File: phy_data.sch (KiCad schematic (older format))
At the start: 18 parts

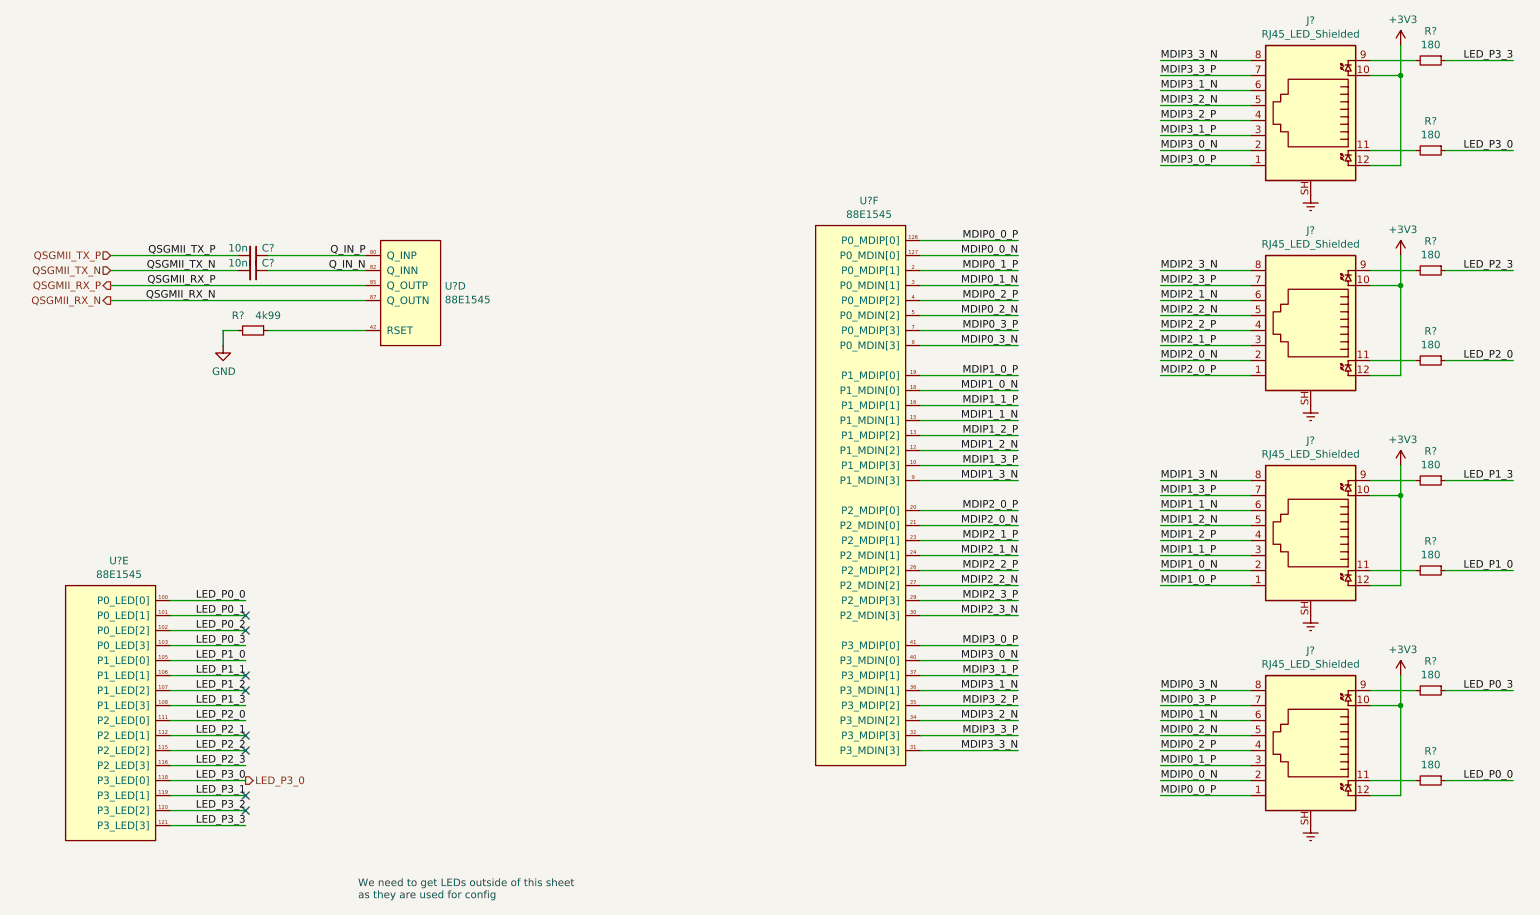
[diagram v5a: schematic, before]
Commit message: sch: Annotate & associate symbols with footprints
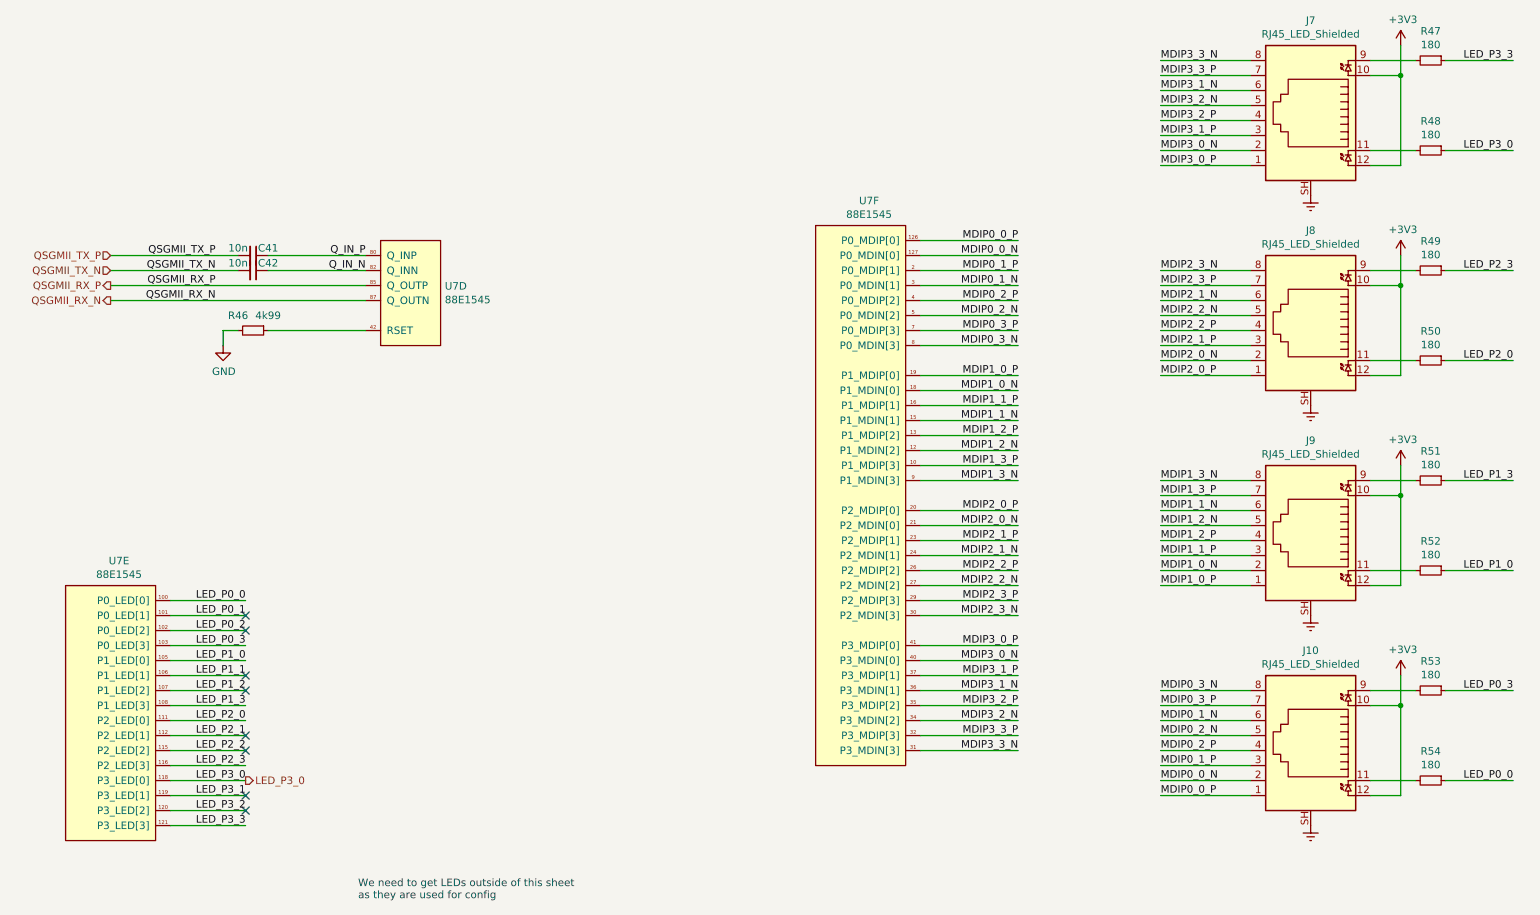
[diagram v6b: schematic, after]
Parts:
- C41, C42: renamed from C?; footprint (none) -> Capacitor_SMD:C_0402_1005Metric
- R46, R47, R48, R49, R50, R51, R52, R53, R54: renamed from R?; footprint (none) -> Resistor_SMD:R_0603_1608Metric
- gave numbers to parts that had none: 5
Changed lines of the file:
@@
 $EndDescr
 $Comp
-L pimouss-motherboard:88E1545 U?
+L pimouss-motherboard:88E1545 U7
 U 4 1 5C7D3D27
 P 3400 2100
-F 0 "U?" H 3828 1796 50  0000 L CNN
+F 0 "U7" H 3828 1796 50  0000 L CNN
 F 1 "88E1545" H 3828 1705 50  0000 L CNN
 F 2 "pimouss-motherboard:LQFP-128-1EP_14x20mm_P0.5mm_EP3.93x6.42mm" H 4850 -300 50  0001 C CNN
@@
 $EndComp
 $Comp
-L pimouss-motherboard:88E1545 U?
+L pimouss-motherboard:88E1545 U7
 U 5 1 5C7D3D6F
 P 1300 4400
-F 0 "U?" H 1656 4565 50  0000 C CNN
+F 0 "U7" H 1656 4565 50  0000 C CNN
 F 1 "88E1545" H 1656 4474 50  0000 C CNN
 F 2 "pimouss-motherboard:LQFP-128-1EP_14x20mm_P0.5mm_EP3.93x6.42mm" H 2750 2000 50  0001 C CNN
@@
 $EndComp
 $Comp
-L pimouss-motherboard:88E1545 U?
+L pimouss-motherboard:88E1545 U7
 U 6 1 5C7D3DC1
 P 6300 2000
-F 0 "U?" H 6656 2165 50  0000 C CNN
+F 0 "U7" H 6656 2165 50  0000 C CNN
 F 1 "88E1545" H 6656 2074 50  0000 C CNN
 F 2 "pimouss-motherboard:LQFP-128-1EP_14x20mm_P0.5mm_EP3.93x6.42mm" H 7750 -400 50  0001 C CNN
@@
 QSGMII_RX_N
 $Comp
-L power:GND #PWR?
+L power:GND #PWR095
 U 1 1 5C7D7B57
 P 2350 2800
-F 0 "#PWR?" H 2350 2550 50  0001 C CNN
+F 0 "#PWR095" H 2350 2550 50  0001 C CNN
 F 1 "GND" H 2355 2627 50  0000 C CNN
 F 2 "" H 2350 2800 50  0001 C CNN
@@
 	2350 2700 2350 2800
 $Comp
-L Connector:RJ45_LED_Shielded J?
+L Connector:RJ45_LED_Shielded J7
 U 1 1 5C7D8260
 P 9600 1300
-F 0 "J?" H 9600 1967 50  0000 C CNN
+F 0 "J7" H 9600 1967 50  0000 C CNN
 F 1 "RJ45_LED_Shielded" H 9600 1876 50  0000 C CNN
 F 2 "Connector_RJ:RJ45_Amphenol_RJHSE538X" V 9600 1325 50  0001 C CNN
@@
 $EndComp
 $Comp
-L Connector:RJ45_LED_Shielded J?
+L Connector:RJ45_LED_Shielded J8
 U 1 1 5C7D8531
 P 9600 2700
-F 0 "J?" H 9600 3367 50  0000 C CNN
+F 0 "J8" H 9600 3367 50  0000 C CNN
 F 1 "RJ45_LED_Shielded" H 9600 3276 50  0000 C CNN
 F 2 "Connector_RJ:RJ45_Amphenol_RJHSE538X" V 9600 2725 50  0001 C CNN
@@
 $EndComp
 $Comp
-L Connector:RJ45_LED_Shielded J?
+L Connector:RJ45_LED_Shielded J9
 U 1 1 5C7D8561
 P 9600 4100
-F 0 "J?" H 9600 4767 50  0000 C CNN
+F 0 "J9" H 9600 4767 50  0000 C CNN
 F 1 "RJ45_LED_Shielded" H 9600 4676 50  0000 C CNN
 F 2 "Connector_RJ:RJ45_Amphenol_RJHSE538X" V 9600 4125 50  0001 C CNN
@@
 $EndComp
 $Comp
-L Connector:RJ45_LED_Shielded J?
+L Connector:RJ45_LED_Shielded J10
 U 1 1 5C7D858F
 P 9600 5500
-F 0 "J?" H 9600 6167 50  0000 C CNN
+F 0 "J10" H 9600 6167 50  0000 C CNN
 F 1 "RJ45_LED_Shielded" H 9600 6076 50  0000 C CNN
 F 2 "Connector_RJ:RJ45_Amphenol_RJHSE538X" V 9600 5525 50  0001 C CNN
@@
 	2500 6000 2000 6000
 $Comp
-L power:+3V3 #PWR?
+L power:+3V3 #PWR0100
 U 1 1 5C918562
 P 10200 800
-F 0 "#PWR?" H 10200 650 50  0001 C CNN
+F 0 "#PWR0100" H 10200 650 50  0001 C CNN
 F 1 "+3V3" H 10215 973 50  0000 C CNN
 F 2 "" H 10200 800 50  0001 C CNN
@@
 	10950 1500 10500 1500
 $Comp
-L power:+3V3 #PWR?
+L power:+3V3 #PWR0101
 U 1 1 5C94B8B0
 P 10200 2200
-F 0 "#PWR?" H 10200 2050 50  0001 C CNN
+F 0 "#PWR0101" H 10200 2050 50  0001 C CNN
 F 1 "+3V3" H 10215 2373 50  0000 C CNN
 F 2 "" H 10200 2200 50  0001 C CNN
@@
 	10950 2900 10500 2900
 $Comp
-L power:+3V3 #PWR?
+L power:+3V3 #PWR0102
 U 1 1 5C950C82
 P 10200 3600
-F 0 "#PWR?" H 10200 3450 50  0001 C CNN
+F 0 "#PWR0102" H 10200 3450 50  0001 C CNN
 F 1 "+3V3" H 10215 3773 50  0000 C CNN
 F 2 "" H 10200 3600 50  0001 C CNN
@@
 	10950 4300 10500 4300
 $Comp
-L power:+3V3 #PWR?
+L power:+3V3 #PWR0103
 U 1 1 5C9567BD
 P 10200 5000
-F 0 "#PWR?" H 10200 4850 50  0001 C CNN
+F 0 "#PWR0103" H 10200 4850 50  0001 C CNN
 F 1 "+3V3" H 10215 5173 50  0000 C CNN
 F 2 "" H 10200 5000 50  0001 C CNN
@@
 	10950 5700 10500 5700
 $Comp
-L power:Earth #PWR?
+L power:Earth #PWR096
 U 1 1 5C96351B
 P 9600 1800
-F 0 "#PWR?" H 9600 1550 50  0001 C CNN
+F 0 "#PWR096" H 9600 1550 50  0001 C CNN
 F 1 "Earth" H 9600 1650 50  0001 C CNN
 F 2 "" H 9600 1800 50  0001 C CNN
@@
 $EndComp
 $Comp
-L power:Earth #PWR?
+L power:Earth #PWR098
 U 1 1 5C963568
 P 9600 4600
-F 0 "#PWR?" H 9600 4350 50  0001 C CNN
+F 0 "#PWR098" H 9600 4350 50  0001 C CNN
 F 1 "Earth" H 9600 4450 50  0001 C CNN
 F 2 "" H 9600 4600 50  0001 C CNN
@@
 $EndComp
 $Comp
-L power:Earth #PWR?
+L power:Earth #PWR097
 U 1 1 5C9635C7
 P 9600 3200
-F 0 "#PWR?" H 9600 2950 50  0001 C CNN
+F 0 "#PWR097" H 9600 2950 50  0001 C CNN
 F 1 "Earth" H 9600 3050 50  0001 C CNN
 F 2 "" H 9600 3200 50  0001 C CNN
@@
 $EndComp
 $Comp
-L power:Earth #PWR?
+L power:Earth #PWR099
 U 1 1 5C9638C0
 P 9600 6000
-F 0 "#PWR?" H 9600 5750 50  0001 C CNN
+F 0 "#PWR099" H 9600 5750 50  0001 C CNN
 F 1 "Earth" H 9600 5850 50  0001 C CNN
 F 2 "" H 9600 6000 50  0001 C CNN
@@
 We need to get LEDs outside of this sheet\nas they are used for config
 $Comp
-L Device:R_Small R?
+L Device:R_Small R47
 U 1 1 5D4C05CB
 P 10400 900
-F 0 "R?" V 10204 900 50  0000 C CNN
+F 0 "R47" V 10204 900 50  0000 C CNN
 F 1 "180" V 10295 900 50  0000 C CNN
-F 2 "" H 10400 900 50  0001 C CNN
+F 2 "Resistor_SMD:R_0603_1608Metric" H 10400 900 50  0001 C CNN
 F 3 "~" H 10400 900 50  0001 C CNN
 	1    10400 900
@@
 $EndComp
 $Comp
-L Device:R_Small R?
+L Device:R_Small R48
 U 1 1 5D4D2934
 P 10400 1500
-F 0 "R?" V 10204 1500 50  0000 C CNN
+F 0 "R48" V 10204 1500 50  0000 C CNN
 F 1 "180" V 10295 1500 50  0000 C CNN
-F 2 "" H 10400 1500 50  0001 C CNN
+F 2 "Resistor_SMD:R_0603_1608Metric" H 10400 1500 50  0001 C CNN
 F 3 "~" H 10400 1500 50  0001 C CNN
 	1    10400 1500
@@
 $EndComp
 $Comp
-L Device:R_Small R?
+L Device:R_Small R49
 U 1 1 5D4DBDE3
 P 10400 2300
-F 0 "R?" V 10204 2300 50  0000 C CNN
+F 0 "R49" V 10204 2300 50  0000 C CNN
 F 1 "180" V 10295 2300 50  0000 C CNN
-F 2 "" H 10400 2300 50  0001 C CNN
+F 2 "Resistor_SMD:R_0603_1608Metric" H 10400 2300 50  0001 C CNN
 F 3 "~" H 10400 2300 50  0001 C CNN
 	1    10400 2300
@@
 $EndComp
 $Comp
-L Device:R_Small R?
+L Device:R_Small R50
 U 1 1 5D4DBDE9
 P 10400 2900
-F 0 "R?" V 10204 2900 50  0000 C CNN
+F 0 "R50" V 10204 2900 50  0000 C CNN
 F 1 "180" V 10295 2900 50  0000 C CNN
-F 2 "" H 10400 2900 50  0001 C CNN
+F 2 "Resistor_SMD:R_0603_1608Metric" H 10400 2900 50  0001 C CNN
 F 3 "~" H 10400 2900 50  0001 C CNN
 	1    10400 2900
@@
 $EndComp
 $Comp
-L Device:R_Small R?
+L Device:R_Small R51
 U 1 1 5D4E554E
 P 10400 3700
-F 0 "R?" V 10204 3700 50  0000 C CNN
+F 0 "R51" V 10204 3700 50  0000 C CNN
 F 1 "180" V 10295 3700 50  0000 C CNN
-F 2 "" H 10400 3700 50  0001 C CNN
+F 2 "Resistor_SMD:R_0603_1608Metric" H 10400 3700 50  0001 C CNN
 F 3 "~" H 10400 3700 50  0001 C CNN
 	1    10400 3700
@@
 $EndComp
 $Comp
-L Device:R_Small R?
+L Device:R_Small R52
 U 1 1 5D4E5554
 P 10400 4300
-F 0 "R?" V 10204 4300 50  0000 C CNN
+F 0 "R52" V 10204 4300 50  0000 C CNN
 F 1 "180" V 10295 4300 50  0000 C CNN
-F 2 "" H 10400 4300 50  0001 C CNN
+F 2 "Resistor_SMD:R_0603_1608Metric" H 10400 4300 50  0001 C CNN
 F 3 "~" H 10400 4300 50  0001 C CNN
 	1    10400 4300
@@
 $EndComp
 $Comp
-L Device:R_Small R?
+L Device:R_Small R53
 U 1 1 5D4E555A
 P 10400 5100
-F 0 "R?" V 10204 5100 50  0000 C CNN
+F 0 "R53" V 10204 5100 50  0000 C CNN
 F 1 "180" V 10295 5100 50  0000 C CNN
-F 2 "" H 10400 5100 50  0001 C CNN
+F 2 "Resistor_SMD:R_0603_1608Metric" H 10400 5100 50  0001 C CNN
 F 3 "~" H 10400 5100 50  0001 C CNN
 	1    10400 5100
@@
 $EndComp
 $Comp
-L Device:R_Small R?
+L Device:R_Small R54
 U 1 1 5D4E5560
 P 10400 5700
-F 0 "R?" V 10204 5700 50  0000 C CNN
+F 0 "R54" V 10204 5700 50  0000 C CNN
 F 1 "180" V 10295 5700 50  0000 C CNN
-F 2 "" H 10400 5700 50  0001 C CNN
+F 2 "Resistor_SMD:R_0603_1608Metric" H 10400 5700 50  0001 C CNN
 F 3 "~" H 10400 5700 50  0001 C CNN
 	1    10400 5700
@@
 $EndComp
 $Comp
-L Device:R_Small R?
+L Device:R_Small R46
 U 1 1 5D4F6574
 P 2550 2700
-F 0 "R?" V 2450 2600 50  0000 C CNN
+F 0 "R46" V 2450 2600 50  0000 C CNN
 F 1 "4k99" V 2450 2800 50  0000 C CNN
-F 2 "" H 2550 2700 50  0001 C CNN
+F 2 "Resistor_SMD:R_0603_1608Metric" H 2550 2700 50  0001 C CNN
 F 3 "~" H 2550 2700 50  0001 C CNN
 	1    2550 2700
@@
 $EndComp
 $Comp
-L Device:C_Small C?
+L Device:C_Small C41
 U 1 1 5D513AC6
 P 2550 2200
-F 0 "C?" V 2500 2300 50  0000 C CNN
+F 0 "C41" V 2500 2300 50  0000 C CNN
 F 1 "10n" V 2500 2100 50  0000 C CNN
-F 2 "" H 2550 2200 50  0001 C CNN
+F 2 "Capacitor_SMD:C_0402_1005Metric" H 2550 2200 50  0001 C CNN
 F 3 "~" H 2550 2200 50  0001 C CNN
 	1    2550 2200
@@
 $EndComp
 $Comp
-L Device:C_Small C?
+L Device:C_Small C42
 U 1 1 5D516975
 P 2550 2300
-F 0 "C?" V 2500 2400 50  0000 C CNN
+F 0 "C42" V 2500 2400 50  0000 C CNN
 F 1 "10n" V 2500 2200 50  0000 C CNN
-F 2 "" H 2550 2300 50  0001 C CNN
+F 2 "Capacitor_SMD:C_0402_1005Metric" H 2550 2300 50  0001 C CNN
 F 3 "~" H 2550 2300 50  0001 C CNN
 	1    2550 2300

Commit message: lib, sch: Fix connectors refdes letter
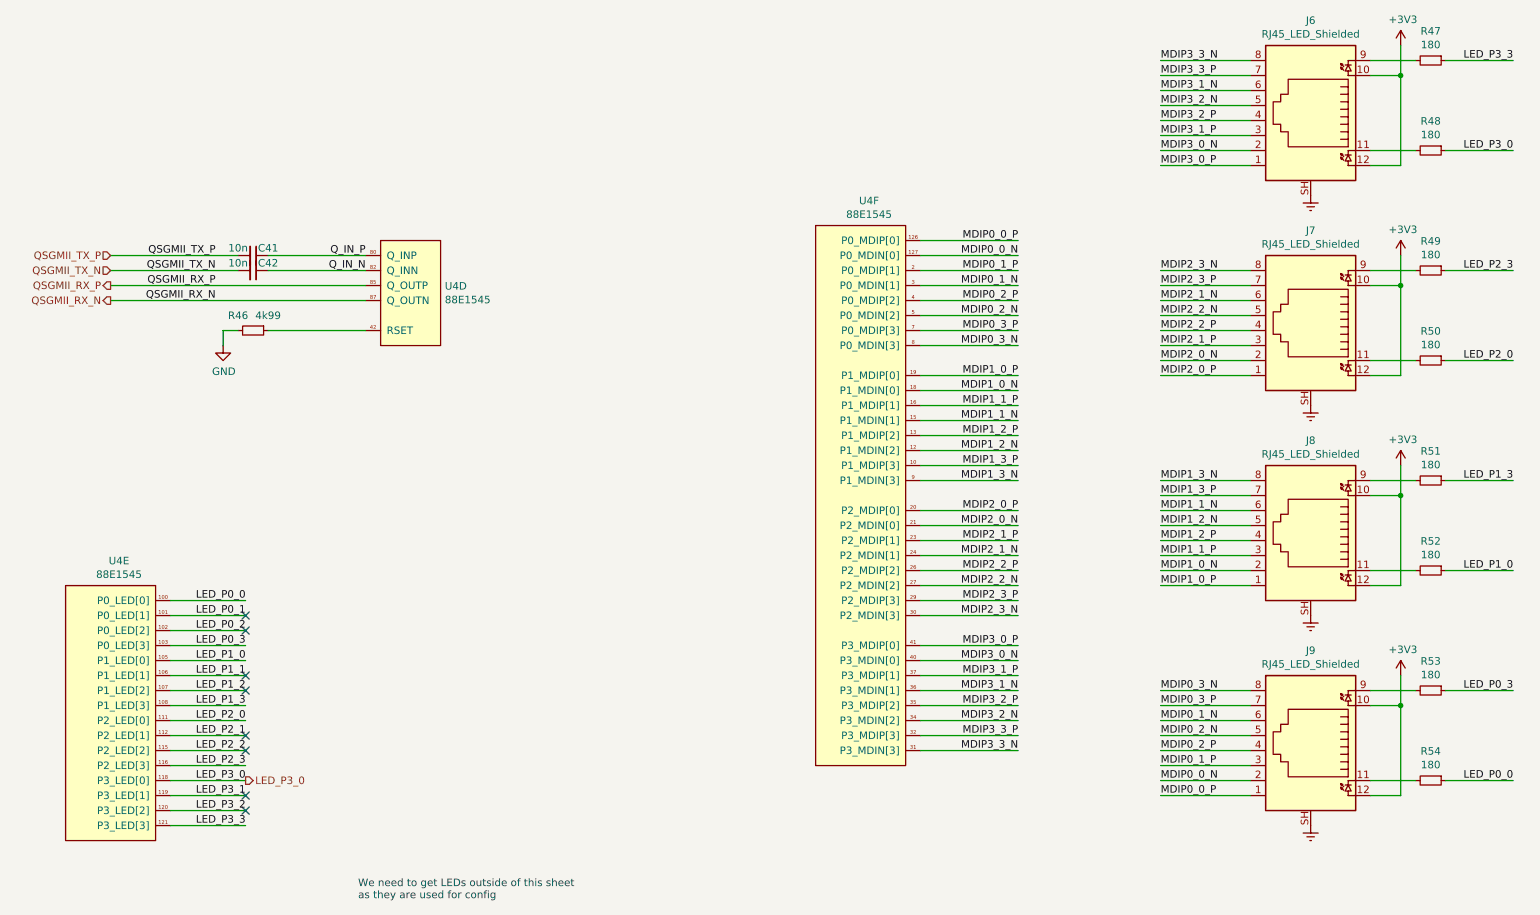
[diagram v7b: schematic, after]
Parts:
- renumbered J7 to J6, J8 to J7, J9 to J8, J10 to J9, U7 to U4
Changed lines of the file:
@@
 $EndDescr
 $Comp
-L pimouss-motherboard:88E1545 U7
+L pimouss-motherboard:88E1545 U4
 U 4 1 5C7D3D27
 P 3400 2100
-F 0 "U7" H 3828 1796 50  0000 L CNN
+F 0 "U4" H 3828 1796 50  0000 L CNN
 F 1 "88E1545" H 3828 1705 50  0000 L CNN
 F 2 "pimouss-motherboard:LQFP-128-1EP_14x20mm_P0.5mm_EP3.93x6.42mm" H 4850 -300 50  0001 C CNN
@@
 $EndComp
 $Comp
-L pimouss-motherboard:88E1545 U7
+L pimouss-motherboard:88E1545 U4
 U 5 1 5C7D3D6F
 P 1300 4400
-F 0 "U7" H 1656 4565 50  0000 C CNN
+F 0 "U4" H 1656 4565 50  0000 C CNN
 F 1 "88E1545" H 1656 4474 50  0000 C CNN
 F 2 "pimouss-motherboard:LQFP-128-1EP_14x20mm_P0.5mm_EP3.93x6.42mm" H 2750 2000 50  0001 C CNN
@@
 $EndComp
 $Comp
-L pimouss-motherboard:88E1545 U7
+L pimouss-motherboard:88E1545 U4
 U 6 1 5C7D3DC1
 P 6300 2000
-F 0 "U7" H 6656 2165 50  0000 C CNN
+F 0 "U4" H 6656 2165 50  0000 C CNN
 F 1 "88E1545" H 6656 2074 50  0000 C CNN
 F 2 "pimouss-motherboard:LQFP-128-1EP_14x20mm_P0.5mm_EP3.93x6.42mm" H 7750 -400 50  0001 C CNN
@@
 	2350 2700 2350 2800
 $Comp
-L Connector:RJ45_LED_Shielded J7
+L Connector:RJ45_LED_Shielded J6
 U 1 1 5C7D8260
 P 9600 1300
-F 0 "J7" H 9600 1967 50  0000 C CNN
+F 0 "J6" H 9600 1967 50  0000 C CNN
 F 1 "RJ45_LED_Shielded" H 9600 1876 50  0000 C CNN
 F 2 "Connector_RJ:RJ45_Amphenol_RJHSE538X" V 9600 1325 50  0001 C CNN
@@
 $EndComp
 $Comp
-L Connector:RJ45_LED_Shielded J8
+L Connector:RJ45_LED_Shielded J7
 U 1 1 5C7D8531
 P 9600 2700
-F 0 "J8" H 9600 3367 50  0000 C CNN
+F 0 "J7" H 9600 3367 50  0000 C CNN
 F 1 "RJ45_LED_Shielded" H 9600 3276 50  0000 C CNN
 F 2 "Connector_RJ:RJ45_Amphenol_RJHSE538X" V 9600 2725 50  0001 C CNN
@@
 $EndComp
 $Comp
-L Connector:RJ45_LED_Shielded J9
+L Connector:RJ45_LED_Shielded J8
 U 1 1 5C7D8561
 P 9600 4100
-F 0 "J9" H 9600 4767 50  0000 C CNN
+F 0 "J8" H 9600 4767 50  0000 C CNN
 F 1 "RJ45_LED_Shielded" H 9600 4676 50  0000 C CNN
 F 2 "Connector_RJ:RJ45_Amphenol_RJHSE538X" V 9600 4125 50  0001 C CNN
@@
 $EndComp
 $Comp
-L Connector:RJ45_LED_Shielded J10
+L Connector:RJ45_LED_Shielded J9
 U 1 1 5C7D858F
 P 9600 5500
-F 0 "J10" H 9600 6167 50  0000 C CNN
+F 0 "J9" H 9600 6167 50  0000 C CNN
 F 1 "RJ45_LED_Shielded" H 9600 6076 50  0000 C CNN
 F 2 "Connector_RJ:RJ45_Amphenol_RJHSE538X" V 9600 5525 50  0001 C CNN
